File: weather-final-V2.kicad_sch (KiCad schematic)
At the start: 45 parts, among them J1 Conn_02x04_Odd_Even, J2 Conn_01x06_Pin, J3 PROGRAMMING_CONN, J4 USB_C_Receptacle_PowerOnly_6P, U1 AMS1117-5.0, U2 ATmega328-P, Y1 Crystal

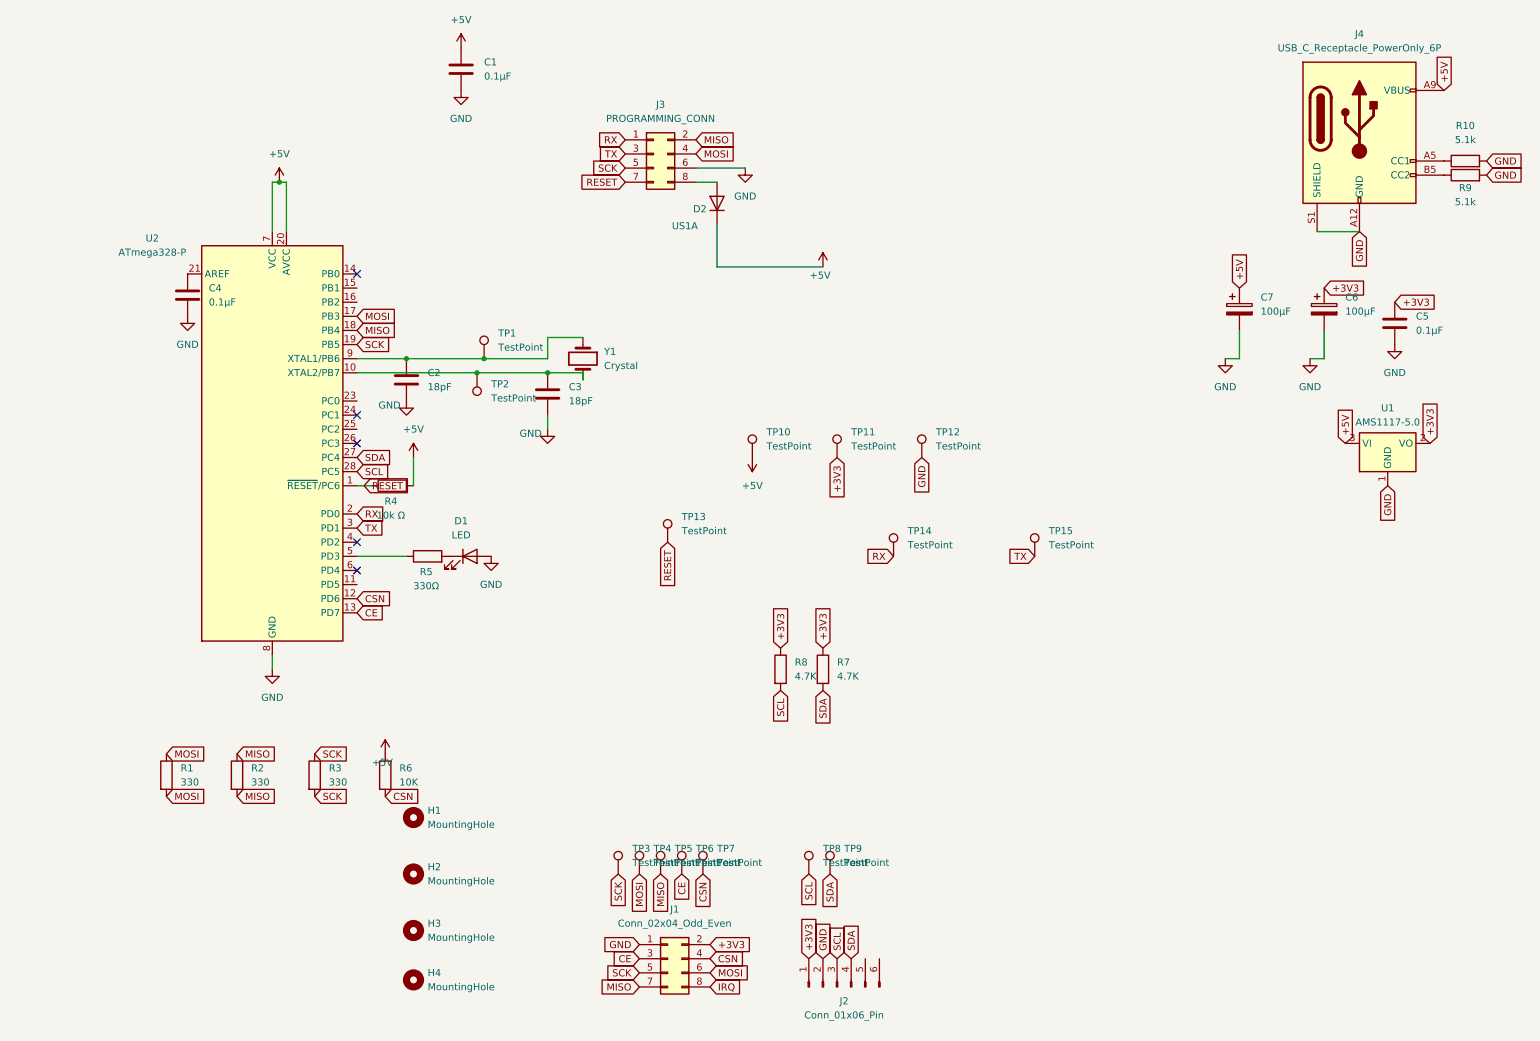
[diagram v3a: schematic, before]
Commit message: Add AVCC decoupling capacitor, Change symbol of 5V to 3V3 converter from AMS1117-5.0 to AMS1117-3.3, Clean up schematics
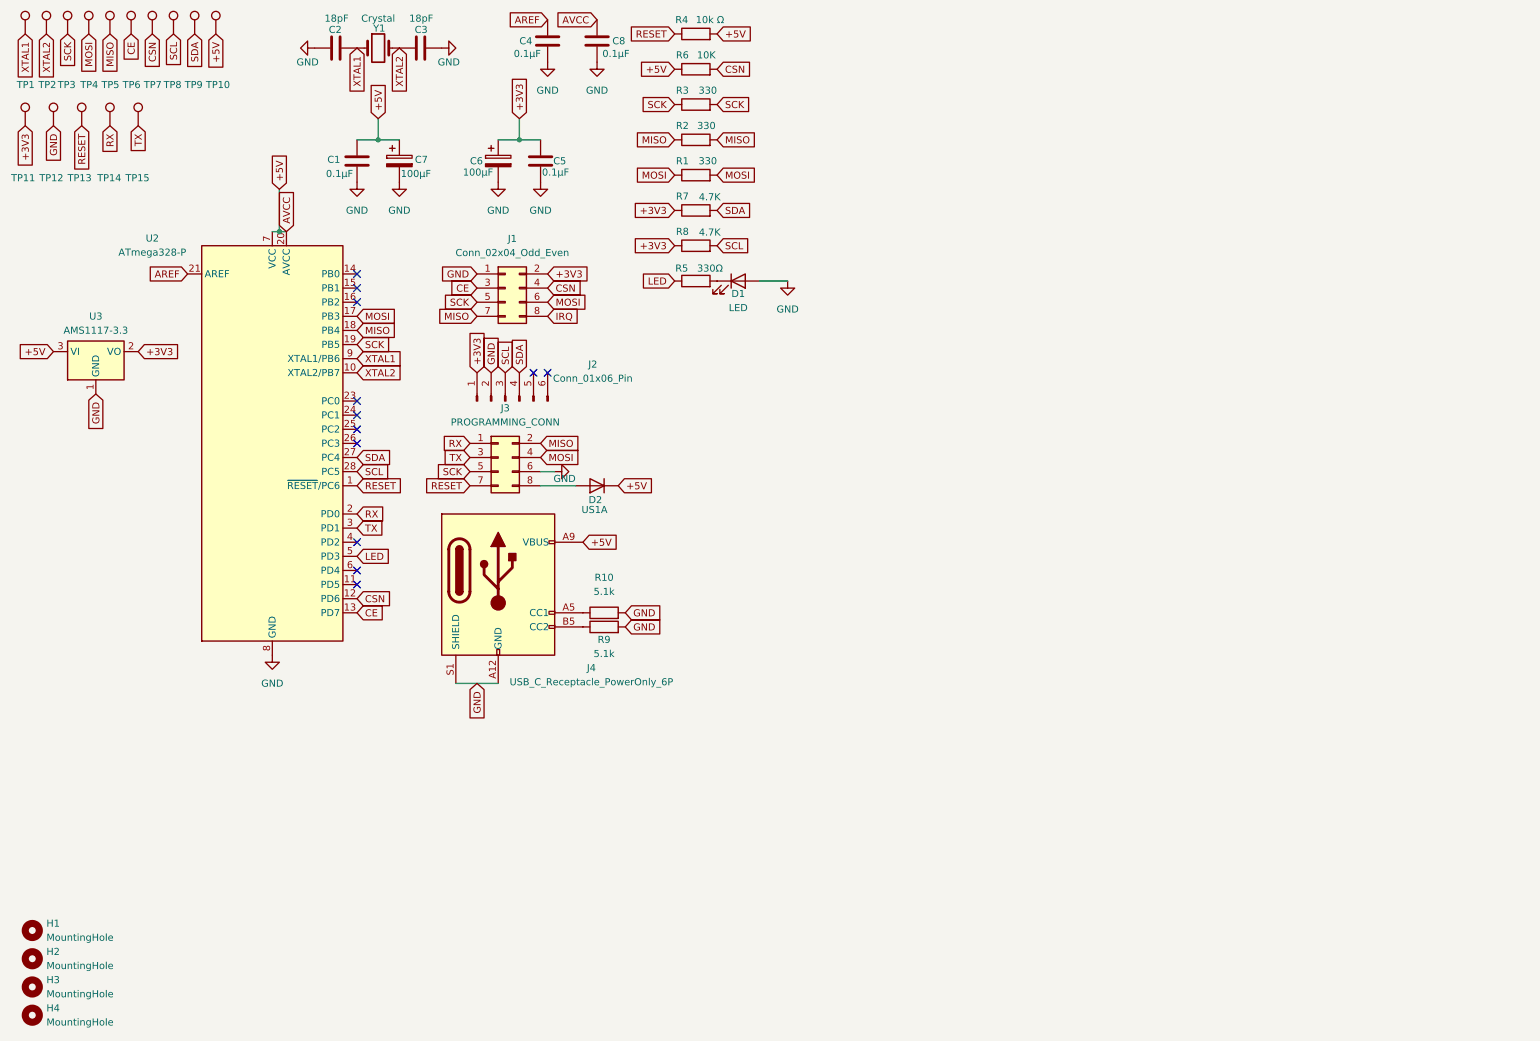
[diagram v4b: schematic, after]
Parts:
- removed U1: AMS1117-5.0, Package_TO_SOT_SMD:SOT-223-3_TabPin2, symbol Regulator_Linear:AMS1117-5.0
- added C8: 0.1μF, Capacitor_SMD:C_1206_3216Metric_Pad1.33x1.80mm_HandSolder, symbol Device:C
- added U3: AMS1117-3.3, Package_TO_SOT_SMD:SOT-223-3_TabPin2, symbol Regulator_Linear:AMS1117-3.3
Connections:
- net +3V3: now also U3.2 (VO)
- net +5V: now also C8.2, U3.3 (VI)
- net GND: now also C8.1, U3.1 (GND)
- net XTAL1: now reaches C2.1, TP1.1, U2.9 (XTAL1/PB6), Y1.1
- net XTAL2: now reaches C3.1, TP2.1, U2.10 (XTAL2/PB7), Y1.2
- net AREF: now reaches C4.1, U2.21 (AREF)
- net LED: now reaches R5.1, U2.5 (PD3)
- no-connect marks 5 -> 12
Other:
- moved on the sheet: C1, C2, C3, C4, C5, C6, C7, D1, D2, H1, H2, H3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
